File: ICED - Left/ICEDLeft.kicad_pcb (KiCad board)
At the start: 2 copper layers, 160.2 x 145 mm, 164 parts, among them P1 FLASH_HDR, P2 USBC, P3 CONN_17, P4 USB3_AFEMALE, Q1 TC1264, U1 MK20DX256VLH7, U2 IS31FL3731C, X1 CRYSTAL

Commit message: renamed S21 and S22 as the initial switch reorganization step
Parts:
- renumbered D23 to D21, D61 to D59, D21 to D81, D22 to D82, D59 to D91, D60 to D92, S23 to S21, S21 to S41, S22 to S82
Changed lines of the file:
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@@
   (net 67 "Net-(D19-Pad1)")
   (net 68 "Net-(D20-Pad1)")
-  (net 69 "Net-(D21-Pad1)")
-  (net 70 "Net-(D22-Pad1)")
-  (net 71 "Net-(D23-Pad1)")
+  (net 69 "Net-(D81-Pad1)")
+  (net 70 "Net-(D82-Pad1)")
+  (net 71 "Net-(D21-Pad1)")
   (net 72 "Net-(D24-Pad1)")
   (net 73 "Net-(D25-Pad1)")
@@
     (add_net "Net-(D2-Pad1)")
     (add_net "Net-(D20-Pad1)")
+    (add_net "Net-(D81-Pad1)")
+    (add_net "Net-(D82-Pad1)")
     (add_net "Net-(D21-Pad1)")
-    (add_net "Net-(D22-Pad1)")
-    (add_net "Net-(D23-Pad1)")
     (add_net "Net-(D24-Pad1)")
     (add_net "Net-(D25-Pad1)")
@@
     (at 160.15609 137.64268 285)
     (attr smd)
-    (fp_text reference D59 (at 0 -1.5 285) (layer B.SilkS)
+    (fp_text reference D91 (at 0 -1.5 285) (layer B.SilkS)
       (effects (font (size 1 1) (thickness 0.2)) (justify mirror))
     )
@@
     (at 93.71645 136.78936 355)
     (attr smd)
-    (fp_text reference D60 (at 0 -1.5 355) (layer B.SilkS)
+    (fp_text reference D92 (at 0 -1.5 355) (layer B.SilkS)
       (effects (font (size 1 1) (thickness 0.2)) (justify mirror))
     )
@@
     (at 149.9952 97.672 270)
     (attr smd)
-    (fp_text reference D61 (at 0 -1.5 270) (layer B.SilkS)
+    (fp_text reference D59 (at 0 -1.5 270) (layer B.SilkS)
       (effects (font (size 1 1) (thickness 0.2)) (justify mirror))
     )
@@
     (tags DIODE)
     (attr smd)
-    (fp_text reference D21 (at 0 3.81 325) (layer B.SilkS)
+    (fp_text reference D81 (at 0 3.81 325) (layer B.SilkS)
       (effects (font (size 1.016 1.016) (thickness 0.2032)) (justify mirror))
     )
@@
       (net 100 /Row4))
     (pad 1 smd rect (at 0 -1.74752 195) (size 1.00076 0.8509) (layers Back B.Paste B.Mask)
-      (net 69 "Net-(D21-Pad1)"))
+      (net 69 "Net-(D81-Pad1)"))
   )
   (module prettylib:SOT123-DIODE (layer Back)
@@
     (tags DIODE)
     (attr smd)
-    (fp_text reference D22 (at 0 3.81 445) (layer B.SilkS)
+    (fp_text reference D82 (at 0 3.81 445) (layer B.SilkS)
       (effects (font (size 1.016 1.016) (thickness 0.2032)) (justify mirror))
     )
@@
       (net 100 /Row4))
     (pad 1 smd rect (at 0 -1.74752 265) (size 1.00076 0.8509) (layers Back B.Paste B.Mask)
-      (net 70 "Net-(D22-Pad1)"))
+      (net 70 "Net-(D82-Pad1)"))
   )
   (module prettylib:SOT123-DIODE (layer Back)
@@
     (tags DIODE)
     (attr smd)
-    (fp_text reference D23 (at 0 3.81 360) (layer B.SilkS)
+    (fp_text reference D21 (at 0 3.81 360) (layer B.SilkS)
       (effects (font (size 1.016 1.016) (thickness 0.2032)) (justify mirror))
     )
@@
       (net 100 /Row4))
     (pad 1 smd rect (at 0 -1.74752 180) (size 1.00076 0.8509) (layers Back B.Paste B.Mask)
-      (net 71 "Net-(D23-Pad1)"))
+      (net 71 "Net-(D21-Pad1)"))
   )
   (module prettylib:SOT123-DIODE (layer Back)
@@
     (descr MXALPS)
     (tags MXALPS)
-    (fp_text reference S22 (at 0 3.048 175) (layer B.SilkS)
+    (fp_text reference S82 (at 0 3.048 175) (layer B.SilkS)
       (effects (font (thickness 0.3048)) (justify mirror))
     )
@@
       (net 121 /Col2))
     (pad 2 thru_hole oval (at 2.52 -4.79 171.1) (size 2.5 3.08) (drill oval 1.5 2.08) (layers *.Cu *.Mask F.SilkS)
-      (net 70 "Net-(D22-Pad1)"))
+      (net 70 "Net-(D82-Pad1)"))
   )
   (module prettylib:MXALPS (layer Front)
@@
     (descr MXALPS)
     (tags MXALPS)
-    (fp_text reference S21 (at 0 3.048 105) (layer B.SilkS)
+    (fp_text reference S41 (at 0 3.048 105) (layer B.SilkS)
       (effects (font (thickness 0.3048)) (justify mirror))
     )
@@
       (net 120 /Col1))
     (pad 2 thru_hole oval (at 2.52 -4.79 101.1) (size 2.5 3.08) (drill oval 1.5 2.08) (layers *.Cu *.Mask F.SilkS)
-      (net 69 "Net-(D21-Pad1)"))
+      (net 69 "Net-(D81-Pad1)"))
   )
   (module prettylib:MXALPS (layer Front)
@@
     (descr MXALPS)
     (tags MXALPS)
-    (fp_text reference S23 (at 0 3.048 90) (layer B.SilkS)
+    (fp_text reference S21 (at 0 3.048 90) (layer B.SilkS)
       (effects (font (thickness 0.3048)) (justify mirror))
     )
@@
       (net 113 /Col3))
     (pad 2 thru_hole oval (at 2.52 -4.79 86.1) (size 2.5 3.08) (drill oval 1.5 2.08) (layers *.Cu *.Mask F.SilkS)
-      (net 71 "Net-(D23-Pad1)"))
+      (net 71 "Net-(D21-Pad1)"))
   )
   (module prettylib:MXALPS (layer Front)

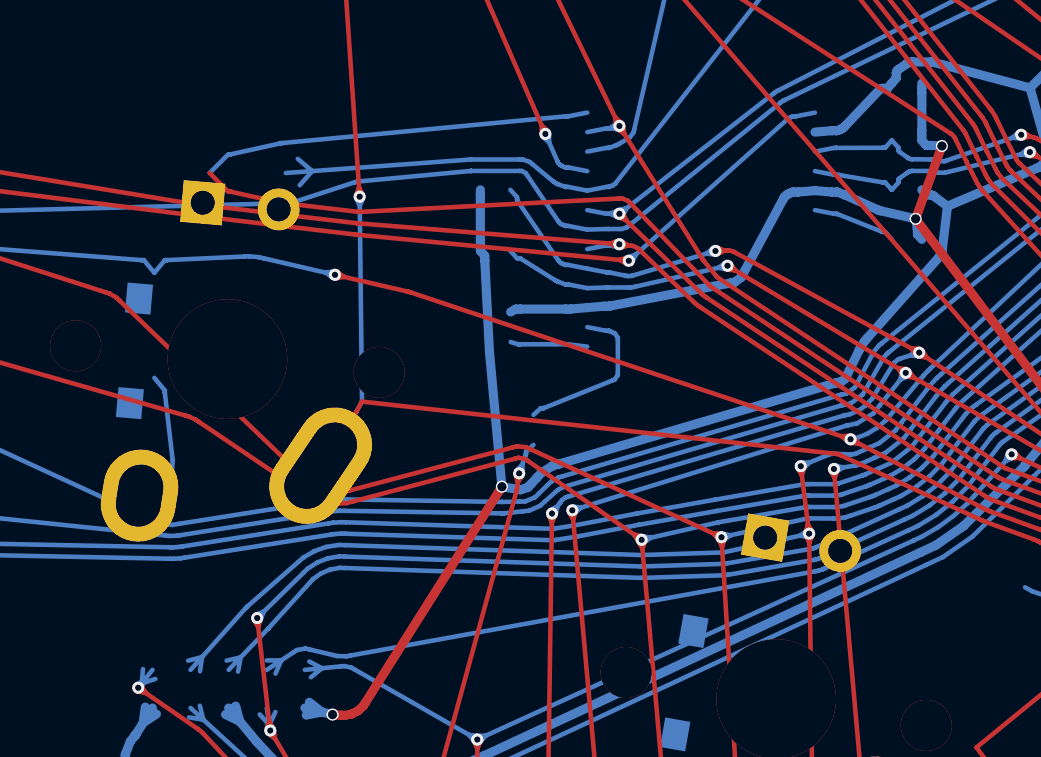
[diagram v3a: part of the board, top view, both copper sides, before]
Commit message: renaming switches ahead of moving the nets
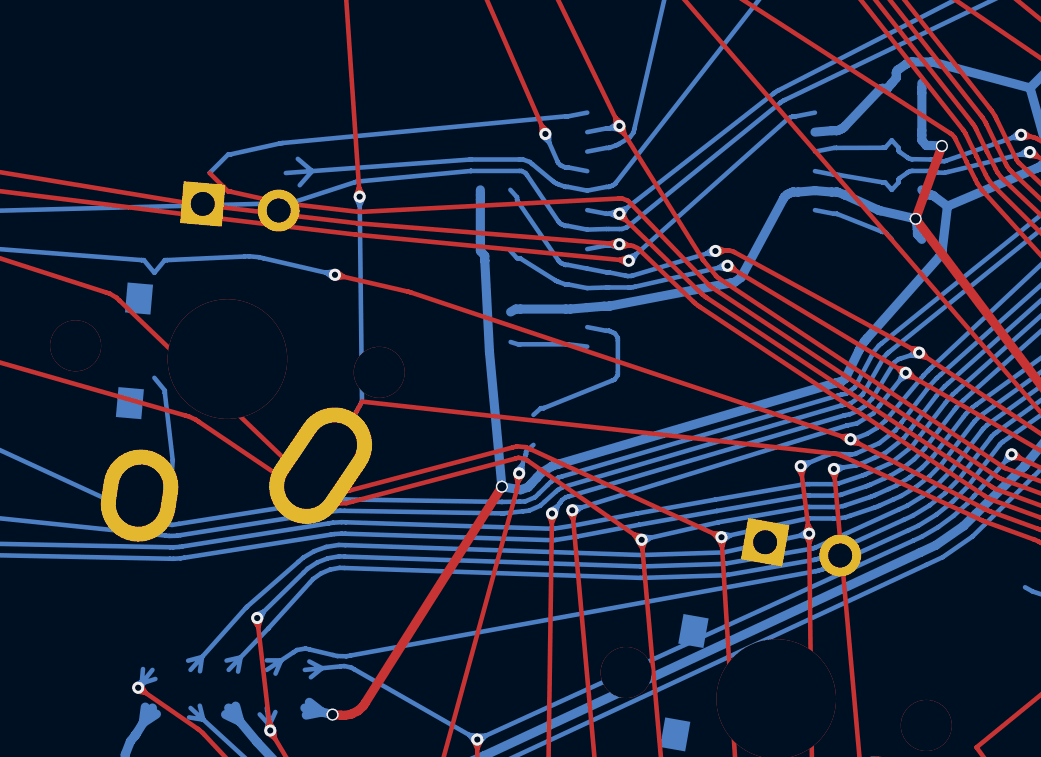
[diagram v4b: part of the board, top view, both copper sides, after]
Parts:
- moved D67 0.15 mm to (125.3, 130.1)
- renumbered D30 to D130, D68 to D168, D24 to D22, D25 to D23, D26 to D24, D27 to D25, D28 to D26, D29 to D27, D32 to D28, D33 to D29, D62 to D60, D63 to D61, D64 to D62, D65 to D63, D66 to D64, D67 to D65, D70 to D66, D71 to D67, S30 to S130, S24 to S22, S25 to S23, S26 to S24, S27 to S25, S28 to S26, S29 to S27, S32 to S28, S33 to S29

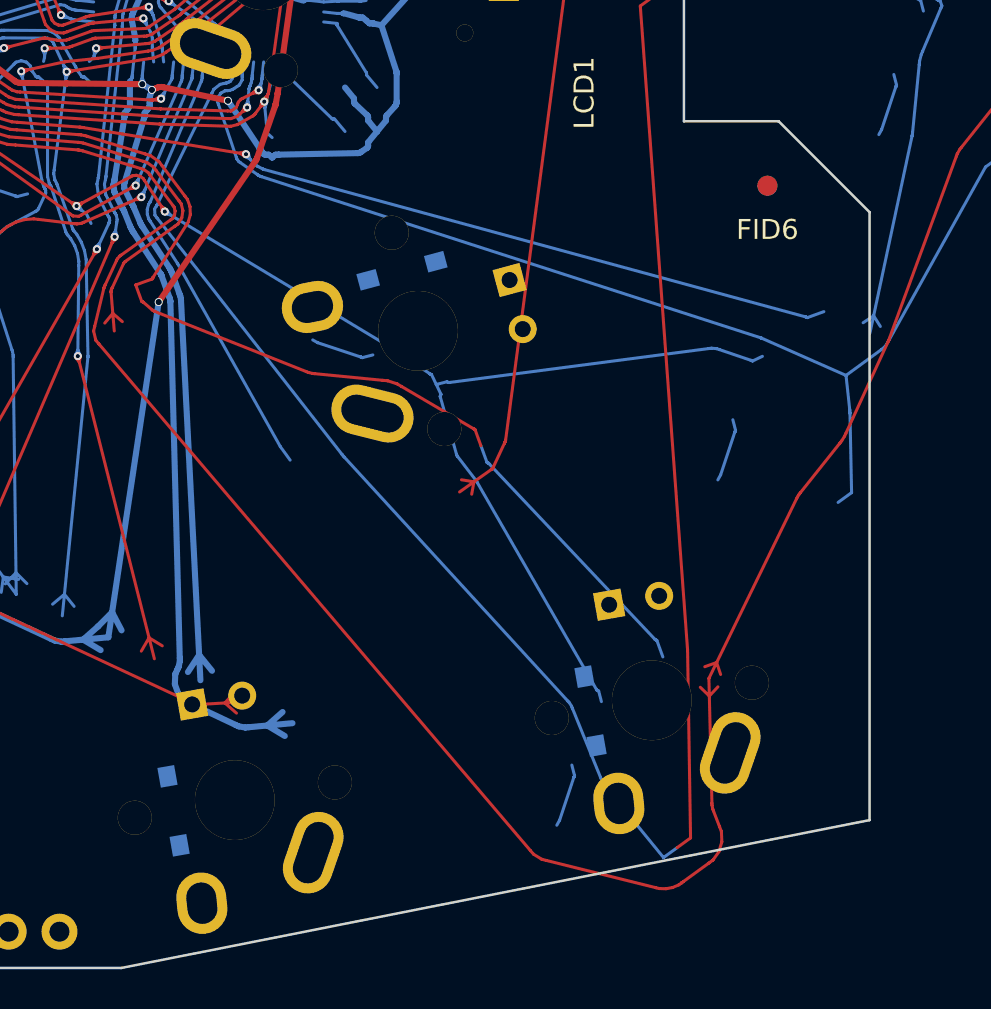
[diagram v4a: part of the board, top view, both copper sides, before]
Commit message: reoredered switch numbering by corrected row and column
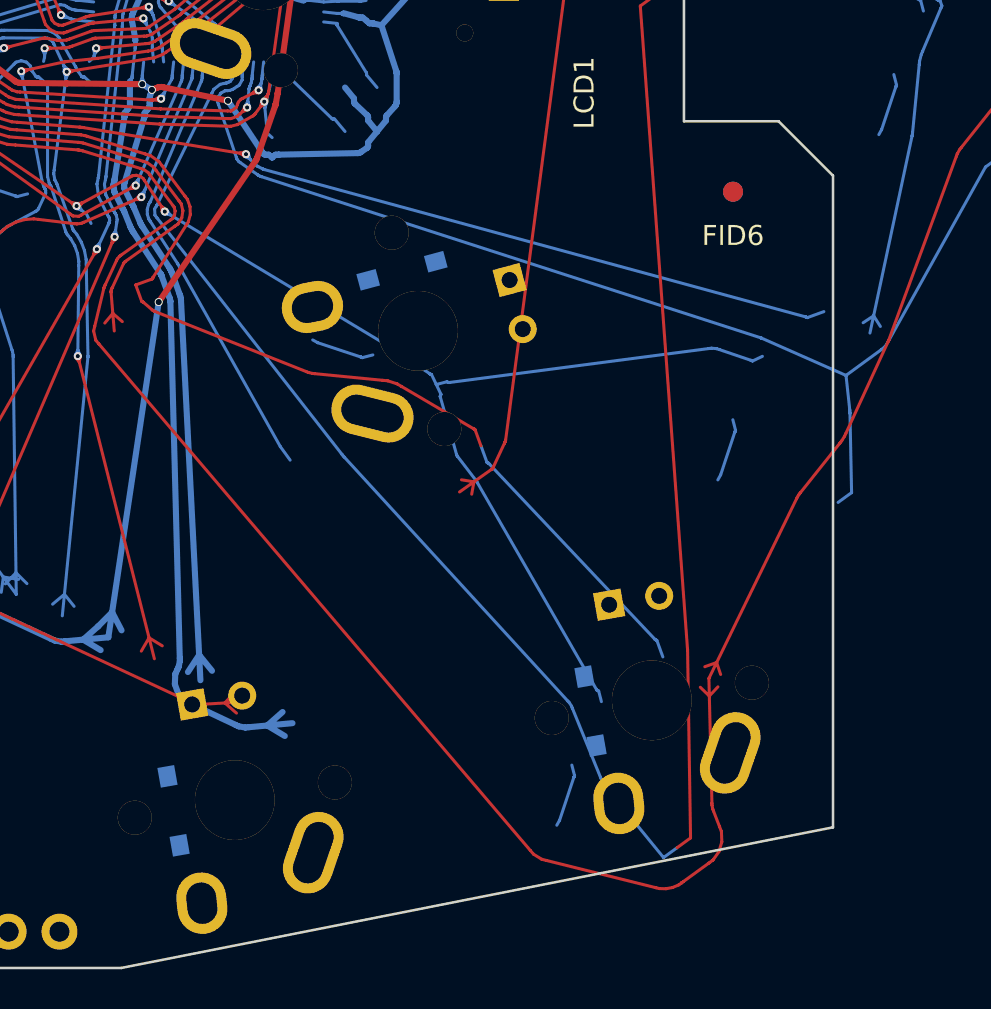
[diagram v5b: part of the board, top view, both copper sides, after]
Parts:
- moved FID5 1.75 mm to (171.0, 132.0)
- moved FID6 1.75 mm to (171.0, 132.0)
- renumbered D21 to D15, D15 to D16, D16 to D17, D17 to D18, D18 to D19, D19 to D20, D20 to D21, D28 to D22, D22 to D23, D23 to D24, D24 to D25, D25 to D26, D26 to D27, D27 to D28, D81 to D29, D29 to D30, D34 to D31, D35 to D32, D37 to D33, D38 to D34, D130 to D35, D31 to D36, D82 to D37, D36 to D38, D59 to D53, D53 to D54, D54 to D55, D55 to D56, D56 to D57, D57 to D58, D58 to D59, D66 to D60, D60 to D61, D61 to D62, D62 to D63, D63 to D64, D64 to D65, D65 to D66, D91 to D67, D67 to D68, D72 to D69, D73 to D70, D75 to D71, D76 to D72, D168 to D73, D69 to D74, D92 to D75, D74 to D76, S21 to S15, S15 to S16, S16 to S17, S17 to S18, S18 to S19, S19 to S20, S20 to S21, S28 to S22, S22 to S23, S23 to S24, S24 to S25, S25 to S26, S26 to S27, S27 to S28, S41 to S29, S29 to S30, S34 to S31, S35 to S32, S37 to S33, S38 to S34, S130 to S35, S31 to S36, S82 to S37, S36 to S38
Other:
- board size 160.2 x 145 mm -> 158.3 x 145 mm
